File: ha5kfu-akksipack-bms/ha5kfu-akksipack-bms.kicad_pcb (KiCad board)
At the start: 2 copper layers, 47 parts, among them IC2 BQ4050RSMR, J1 PACK, J2 PACK1, J3 PACK2, J4 COM, Q1 AON6512, Q2 AON6512, Q3 2N7002, Q4 AO3400A, Q5 AO3400A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

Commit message: Add initial PCB design
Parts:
- removed 100n1: C, Capacitor_SMD:C_0805_2012Metric_Pad1.18x1.45mm_HandSolder
- removed IC2: BQ4050RSMR, BQ4050:QFN40P400X400X100-33N-D
- added C10: 100n, Capacitor_SMD:C_0603_1608Metric_Pad1.08x0.95mm_HandSolder, B.Cu at (128.3, 124.2)
- added IC1: BQ4050RSMR, Package_DFN_QFN:VQFN-32-1EP_4x4mm_P0.4mm_EP2.8x2.8mm, F.Cu at (123.8, 108.6)
- added R23: 100, Resistor_SMD:R_0603_1608Metric_Pad0.98x0.95mm_HandSolder, B.Cu at (127.5, 126.6)
- C1, C2, C3, C4, C5, C6, C7, C8: footprint Capacitor_SMD:C_0805_2012Metric_Pad1.18x1.45mm_HandSolder -> Capacitor_SMD:C_0603_1608Metric_Pad1.08x0.95mm_HandSolder
- J1: footprint Connector_Wire:SolderWire-0.75sqmm_1x02_P4.8mm_D1.25mm_OD2.3mm -> Connector_AMASS:AMASS_XT30U-F_1x02_P5.0mm_Vertical
- J2, J3: footprint Connector_JST:JST_PH_B3B-PH-K_1x03_P2.00mm_Vertical -> Connector_JST:JST_PH_S3B-PH-K_1x03_P2.00mm_Horizontal
- R1, R22: footprint Resistor_SMD:R_0805_2012Metric_Pad1.20x1.40mm_HandSolder -> Resistor_SMD:R_0603_1608Metric_Pad0.98x0.95mm_HandSolder; moved to B.Cu
- R10, R11, R13, R15, R16, R2, R3, R6, R7: footprint Resistor_SMD:R_0805_2012Metric_Pad1.20x1.40mm_HandSolder -> Resistor_SMD:R_0603_1608Metric_Pad0.98x0.95mm_HandSolder
- R12, R14, R17, R4, R5, R8, R9: footprint Resistor_SMD:R_1206_3216Metric -> Resistor_SMD:R_0603_1608Metric_Pad0.98x0.95mm_HandSolder
- R18: value 100 -> 10k; footprint Resistor_SMD:R_0805_2012Metric_Pad1.20x1.40mm_HandSolder -> Resistor_SMD:R_0603_1608Metric_Pad0.98x0.95mm_HandSolder
- R19: value 33 -> 100; footprint Resistor_SMD:R_1206_3216Metric -> Resistor_SMD:R_0603_1608Metric_Pad0.98x0.95mm_HandSolder
- R20: value 0.001 -> 33; footprint Resistor_SMD:R_1206_3216Metric -> Resistor_SMD:R_0603_1608Metric_Pad0.98x0.95mm_HandSolder
- R21: value 100 -> 0.001; footprint Resistor_SMD:R_0805_2012Metric_Pad1.20x1.40mm_HandSolder -> Resistor_SMD:R_1206_3216Metric_Pad1.30x1.75mm_HandSolder; moved to B.Cu
- moved R3 85.4 mm to (120.7, 116.7)
- moved Q3 79.8 mm to (123.5, 116.7), turned to 0 degrees
- moved R7 72.6 mm to (121.6, 114.1), turned to 180 degrees
- moved R11 72.4 mm to (126.5, 117.0), turned to 90 degrees
- moved R10 71.8 mm to (128.9, 116.1), turned to 180 degrees
- moved R2 69.5 mm to (128.8, 121.5)
- moved Q2 67.8 mm to (133.2, 121.3), turned to 0 degrees
- moved R16 66.5 mm to (120.4, 106.7), turned to 90 degrees
- moved R6 61.4 mm to (128.3, 114.6), turned to 180 degrees
- moved C2 61.4 mm to (135.0, 117.6)
- moved C1 61.1 mm to (139.2, 117.6)
- moved C9 57.8 mm to (127.4, 111.9), turned to -90 degrees
- moved J2 55.9 mm to (139.8, 126.1), turned to 0 degrees
- moved D1 55.5 mm to (132.8, 115.1), turned to 0 degrees
- moved Q1 54.1 mm to (141.1, 121.3), turned to 180 degrees
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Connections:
- J2 pad 1: Net-(D1-A) -> Net-(J2-Pin_1)
- J2 pad 3: Net-(J2-Pin_3) -> Net-(D1-A)
- J3 pad 1: Net-(J2-Pin_3) -> GND
- J3 pad 3: GND -> Net-(J2-Pin_1)
- Q5 pad 2: Net-(J2-Pin_3) -> Net-(J2-Pin_1)
- R12 pad 1: Net-(J2-Pin_3) -> Net-(J2-Pin_1)
- R14 pad 1: Net-(J2-Pin_3) -> Net-(J2-Pin_1)
- R18 pad 1: Net-(IC2-~{PRES}/~{SHDN}) -> GND
- R19 pad 1: Net-(Q7-S) -> Net-(IC1-~{PRES}/~{SHDN})
- R19 pad 2: GND -> /~{SHDN}
- R20 pad 1: GND -> Net-(Q7-S)
- R20 pad 2: /PACK- -> GND
- R21 pad 1: Net-(IC2-SRP) -> GND
- R21 pad 2: GND -> /PACK-
- R22 pad 2: /PACK- -> GND
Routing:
- net Net-(D1-A): track 0.00 -> 35.6 mm, vias 0 -> 2
- net Net-(J2-Pin_1): track 0.00 -> 25.3 mm, vias 0 -> 1
- net Net-(IC1-VC3): track 0.00 -> 23.4 mm, vias 0 -> 2
- net Net-(IC1-SRP): track 0.00 -> 22.7 mm, vias 0 -> 1
- net /PACK+: track 0.00 -> 22.4 mm
- net Net-(Q1-G): track 0.00 -> 21.1 mm, vias 0 -> 2
- net Net-(IC1-VC4): track 0.00 -> 21.1 mm, vias 0 -> 2
- net Net-(IC1-SRN): track 0.00 -> 21.0 mm, vias 0 -> 1
- net GND: track 0.00 -> 19.9 mm, vias 0 -> 7
- net /PACK-: track 0.00 -> 19.4 mm
- net Net-(Q1-D): track 0.00 -> 19.4 mm, vias 0 -> 2
- net Net-(IC1-VC2): track 0.00 -> 19.3 mm, vias 0 -> 2
- net Net-(J2-Pin_2): track 0.00 -> 19.3 mm, vias 0 -> 1
- net Net-(J3-Pin_2): track 0.00 -> 19.1 mm, vias 0 -> 1
- net Net-(IC1-VC1): track 0.00 -> 17.8 mm
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- added copper zone on F.Cu, net /PACK+
- added copper zone on B.Cu, net GND
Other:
- board outline added: 26.6 x 40.7 mm

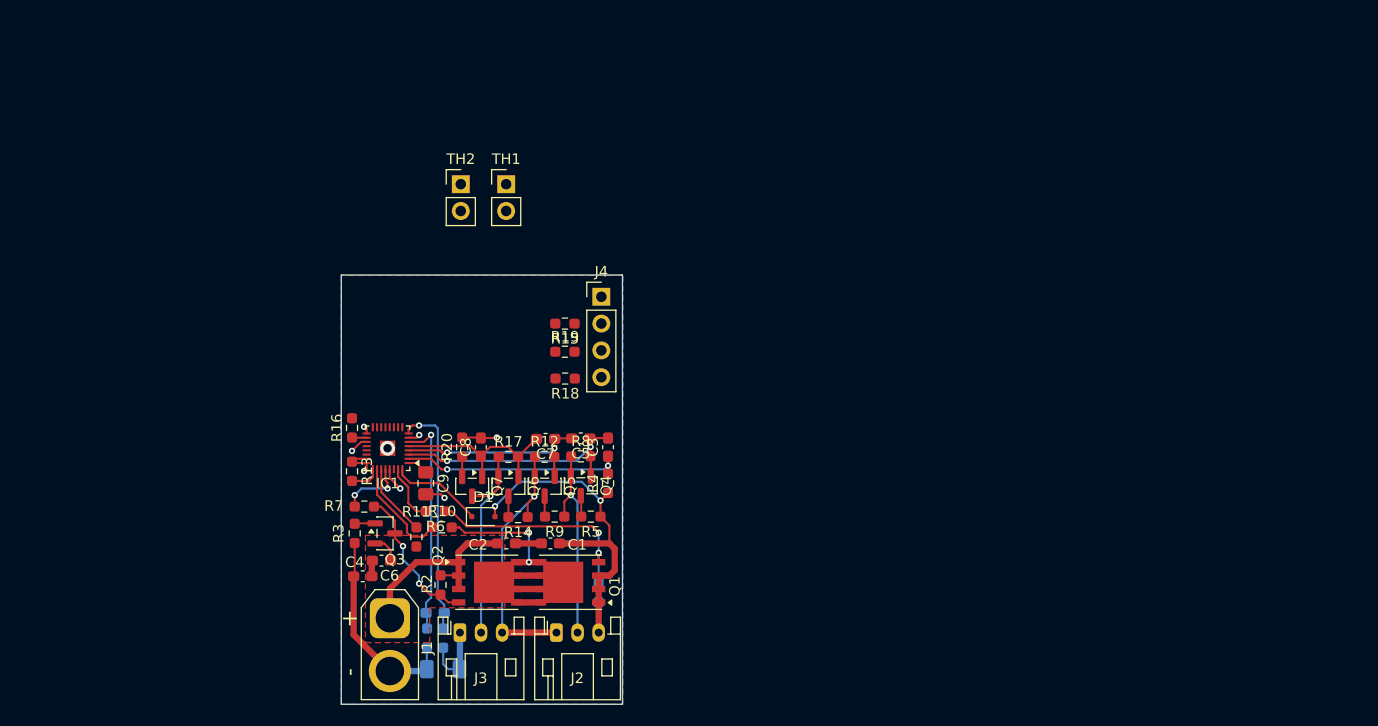
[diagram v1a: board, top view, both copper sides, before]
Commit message: Add LEDs, modify PCB
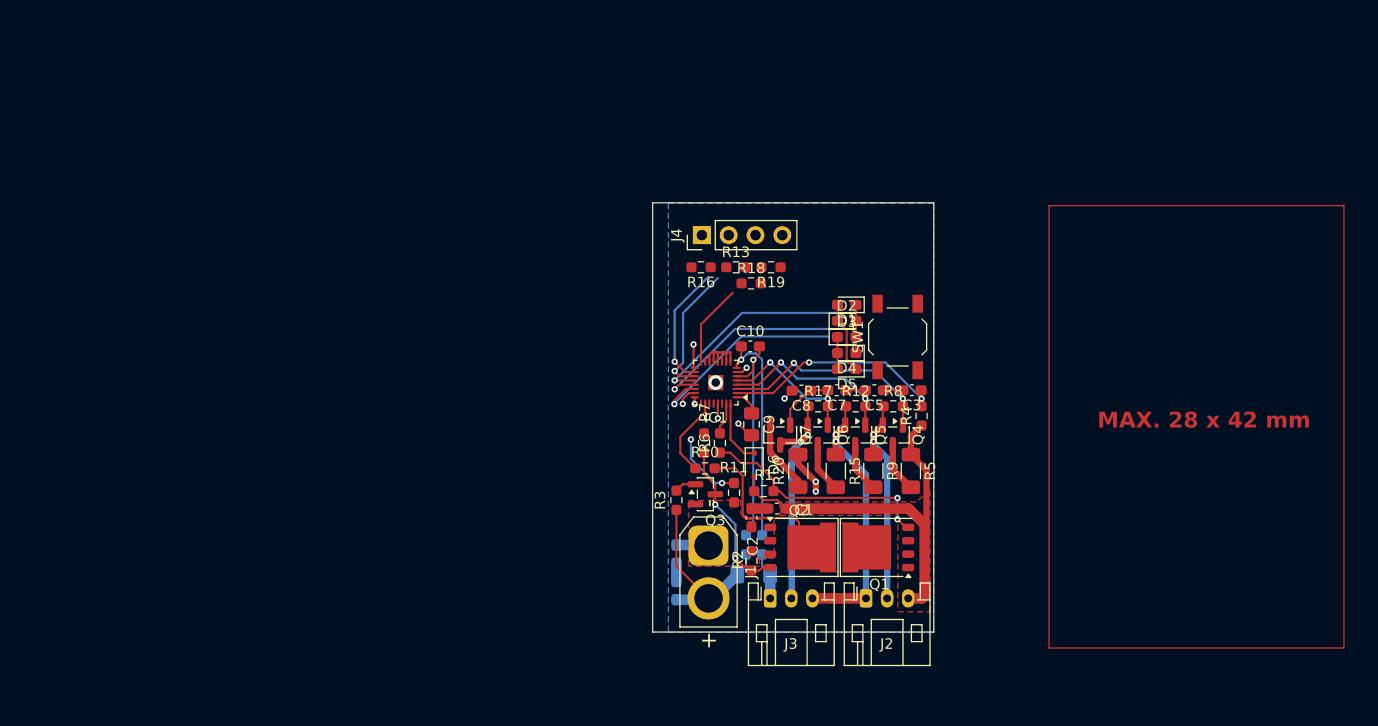
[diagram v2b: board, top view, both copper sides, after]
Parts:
- removed R14: 33, Resistor_SMD:R_0603_1608Metric_Pad0.98x0.95mm_HandSolder
- removed TH1, TH2: 10k -- 3450K, Connector_PinHeader_2.54mm:PinHeader_1x02_P2.54mm_Vertical
- added D2: LED2, LED_SMD:LED_0603_1608Metric_Pad1.05x0.95mm_HandSolder, F.Cu at (167.3, 96.5)
- added D3: LED3, LED_SMD:LED_0603_1608Metric_Pad1.05x0.95mm_HandSolder, F.Cu at (167.3, 98.0)
- added D4: LED4, LED_SMD:LED_0603_1608Metric_Pad1.05x0.95mm_HandSolder, F.Cu at (167.3, 99.6)
- added D5: LED5, LED_SMD:LED_0603_1608Metric_Pad1.05x0.95mm_HandSolder, F.Cu at (167.3, 101.1)
- added D6: BAT54, Diode_SMD:D_SOD-323F, F.Cu at (158.5, 110.2)
- added SW1: DISP, Button_Switch_SMD:SW_SPST_TL3342, F.Cu at (172.1, 98.0)
- C10, R1: moved to F.Cu
- C4, C6: moved to B.Cu
- D1: value BAT54 -> LED1; footprint Diode_SMD:D_SOD-323F -> LED_SMD:LED_0603_1608Metric_Pad1.05x0.95mm_HandSolder
- Q1, Q2: footprint Package_SO:PowerPAK_SO-8_Single -> Package_DFN_QFN:PQFN-8-EP_6x5mm_P1.27mm_Generic
- R11: value 10k -> 10k precision
- R13: value 0 -> 100
- R15: value 100 -> 33; footprint Resistor_SMD:R_0603_1608Metric_Pad0.98x0.95mm_HandSolder -> Resistor_SMD:R_1206_3216Metric_Pad1.30x1.75mm_HandSolder
- R18: value 10k -> 100
- R19: value 100 -> 10k
- R20, R5, R9: footprint Resistor_SMD:R_0603_1608Metric_Pad0.98x0.95mm_HandSolder -> Resistor_SMD:R_1206_3216Metric_Pad1.30x1.75mm_HandSolder
- moved R13 41.2 mm to (156.8, 91.4), turned to 0 degrees
- moved D1 39.8 mm to (167.3, 95.0), turned to 180 degrees
- moved C10 39.1 mm to (158.1, 98.9), turned to 0 degrees
- moved R16 36.4 mm to (153.5, 91.4), turned to 180 degrees
- moved R7 32.7 mm to (153.8, 108.1), turned to 90 degrees
- moved R20 31.9 mm to (162.7, 110.7)
- moved IC1 31.7 mm to (154.9, 102.4)
- moved R23 31.5 mm to (157.7, 117.7)
- moved R22 31.5 mm to (159.3, 117.7)
- moved C9 31.4 mm to (158.2, 106.3)
- moved J1 31.0 mm to (154.2, 117.8)
- moved C8 30.8 mm to (163.0, 103.1), turned to 180 degrees
- moved R21 30.8 mm to (158.5, 120.5)
- moved R3 30.6 mm to (151.1, 113.5)
- moved R5 30.6 mm to (173.3, 110.7), turned to -90 degrees
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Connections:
- net /~{SHDN} renamed /~{PRES}
- C1 pad 1: Net-(D1-A) -> Net-(D6-A)
- IC1 pad 10: Net-(IC1-TS1) -> GND
- IC1 pad 11: Net-(IC1-TS2) -> GND
- IC1 pad 17: GND -> Net-(IC1-~{DISP})
- IC1 pad 20: unconnected-(IC1-LEDCNTLA-Pad20) -> Net-(D1-A)
- IC1 pad 21: unconnected-(IC1-LEDCNTLB-Pad21) -> Net-(D1-K)
- IC1 pad 22: unconnected-(IC1-LEDCNTLC-Pad22) -> Net-(D3-K)
- IC1 pad 25: Net-(IC1-FUSE) -> unconnected-(IC1-FUSE-Pad25)
- IC1 pad 32: Net-(D1-K) -> Net-(D6-K)
- J2 pad 3: Net-(D1-A) -> Net-(D6-A)
- Q1 pad 1: Net-(D1-A) -> Net-(D6-A)
- Q1 pad 2: Net-(D1-A) -> Net-(D6-A)
- Q1 pad 3: Net-(D1-A) -> Net-(D6-A)
- R1 pad 1: Net-(D1-A) -> Net-(D6-A)
- R13 pad 1: GND -> /SMB_SCL
- R13 pad 2: Net-(IC1-FUSE) -> Net-(IC1-SMBC)
- R15 pad 1: /SMB_SCL -> Net-(J2-Pin_1)
- R15 pad 2: Net-(IC1-SMBC) -> Net-(Q6-D)
- R18 pad 1: GND -> Net-(IC1-~{PRES}/~{SHDN})
- R19 pad 1: Net-(IC1-~{PRES}/~{SHDN}) -> GND
- R4 pad 1: Net-(D1-A) -> Net-(D6-A)
- R5 pad 1: Net-(D1-A) -> Net-(D6-A)
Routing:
- net Net-(D6-A): track 0.00 -> 37.7 mm
- net Net-(D3-K): track 0.00 -> 23.1 mm, vias 0 -> 1
- net /PACK+: track 22.4 -> 3.07 mm
- net Net-(D1-K): track 8.81 -> 26.2 mm, vias 0 -> 1
- net Net-(IC1-SMBC): track 1.73 -> 12.6 mm
- net Net-(IC1-SMBD): track 1.39 -> 11.7 mm, vias 0 -> 1
- net Net-(D1-A): track 35.6 -> 26.7 mm, vias 2 -> 1
- net Net-(IC1-~{PRES}/~{SHDN}): track 0.00 -> 7.77 mm
- net Net-(IC1-DSG): track 6.37 -> 0.00 mm, vias 2 -> 0
- net Net-(D6-K): track 0.00 -> 6.19 mm
- net Net-(Q7-S): track 1.86 -> 7.00 mm
- net Net-(Q1-D): track 19.4 -> 14.6 mm, vias 2 -> 0
- net GND: track 19.9 -> 23.6 mm, vias 7 -> 9
- net Net-(IC1-FUSE): track 2.86 -> 0.00 mm
- net Net-(J3-Pin_2): track 19.1 -> 21.9 mm, vias 1 -> 2
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- added copper zone on F.Cu, net Net-(D6-A)
- added copper zone on F.Cu, net Net-(Q1-D)
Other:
- board text added: "MAX. 28 x 42 mm"

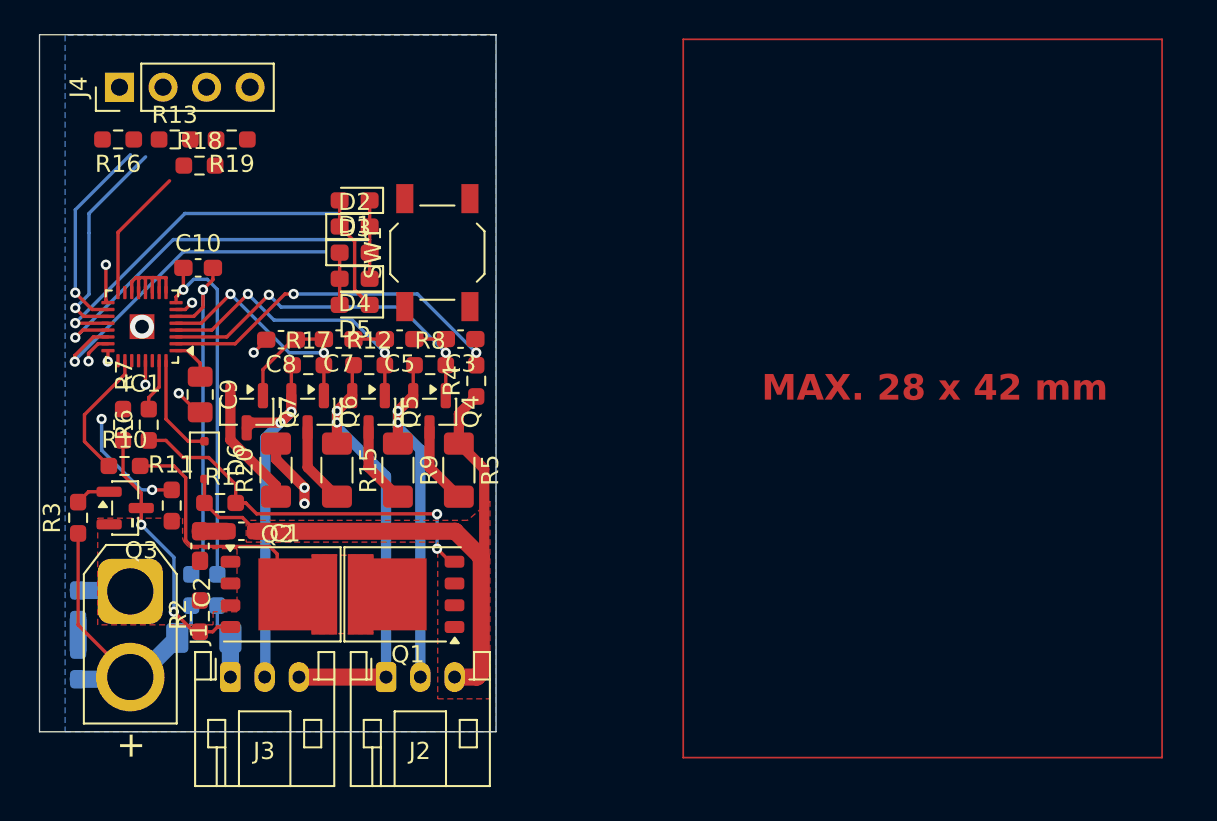
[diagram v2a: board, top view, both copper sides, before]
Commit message: Complete PCB, add comments (as documentation) to schematic
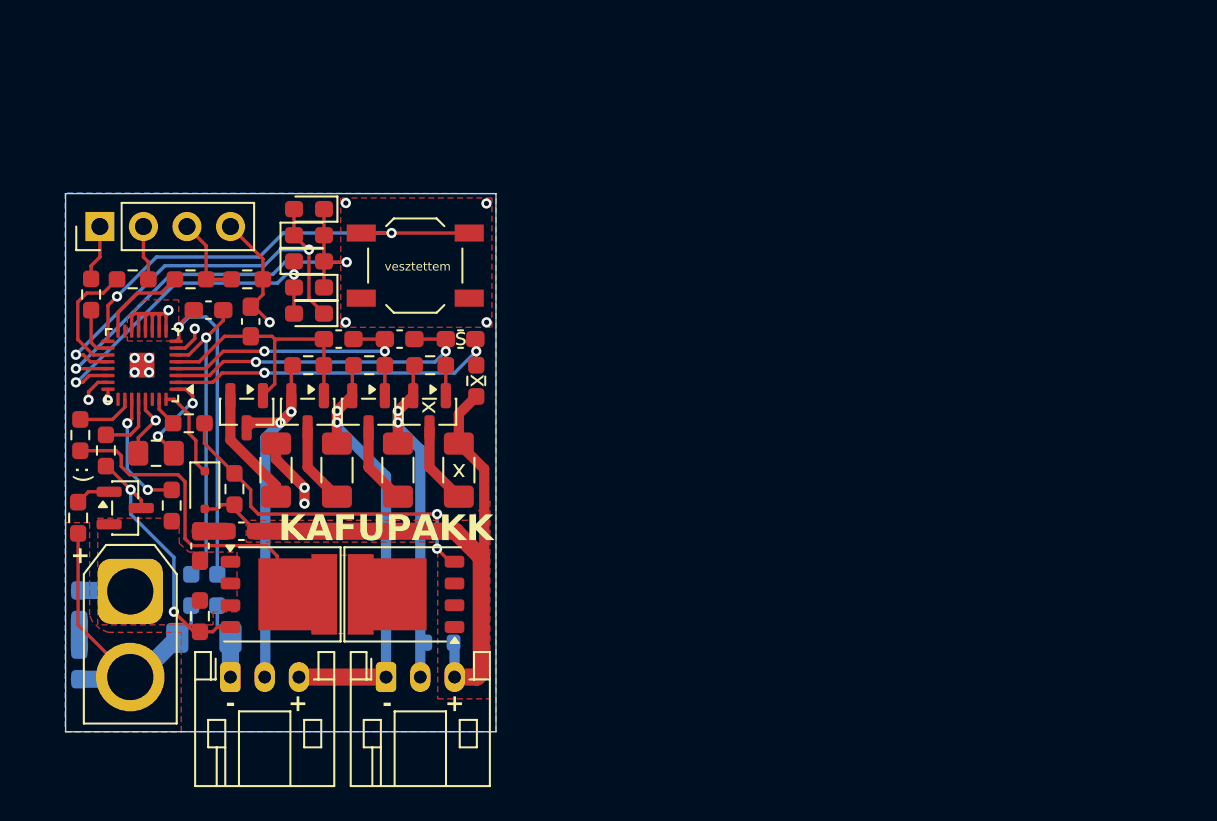
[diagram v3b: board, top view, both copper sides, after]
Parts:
- added BT1: LiFePO4, Resistor_SMD:R_0603_1608Metric, B.Cu at (172.2, 120.8)
- moved R16 9.18 mm to (151.9, 100.5), turned to 90 degrees
- moved R13 8.52 mm to (154.3, 99.6), turned to 180 degrees
- moved R19 8.21 mm to (161.0, 99.6)
- moved J4 8.21 mm to (152.4, 96.5)
- moved R18 6.66 mm to (157.7, 99.6)
- moved C9 4.29 mm to (155.7, 109.8), turned to 180 degrees
- moved R10 3.15 mm to (151.3, 108.7), turned to 90 degrees
- moved D1 2.71 mm to (164.6, 95.5)
- moved D2 2.71 mm to (164.6, 97.0)
- moved D3 2.71 mm to (164.6, 98.6)
- moved D4 2.71 mm to (164.6, 100.1)
- moved D5 2.71 mm to (164.6, 101.6)
- moved C10 2.54 mm to (158.7, 101.4)
- moved R6 2.34 mm to (157.6, 108.0), turned to 180 degrees
- moved IC1 2.25 mm to (154.9, 104.6)
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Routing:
- net Net-(IC1-~{DISP}): track 2.26 -> 26.7 mm, vias 1 -> 2
- net GND: track 23.6 -> 33.2 mm, vias 9 -> 16
- net Net-(IC1-SMBD): track 11.7 -> 3.00 mm, vias 1 -> 0
- net Net-(IC1-SMBC): track 12.6 -> 7.16 mm, vias 1 -> 0
- net /~{PRES}: track 0.00 -> 5.03 mm
- net Net-(IC1-VCC): track 7.71 -> 3.36 mm
- net Net-(Q1-D): track 14.6 -> 18.6 mm
- net Net-(IC1-DSG): track 0.00 -> 3.80 mm
- net Net-(IC1-VC1): track 19.9 -> 16.2 mm, vias 2 -> 0
- net Net-(IC1-PBI): track 2.49 -> 5.91 mm, vias 0 -> 2
- net /SMB_SDA: track 0.00 -> 3.27 mm
- net /SMB_SCL: track 0.00 -> 3.20 mm
- net Net-(IC1-SRN): track 21.2 -> 18.4 mm
- net Net-(D3-K): track 23.1 -> 20.4 mm, vias 1 -> 2
- net Net-(IC1-~{PRES}/~{SHDN}): track 7.77 -> 5.20 mm
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- added copper zone on F.Cu, net /PACK-
- added copper zone on F.Cu, net GND
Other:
- board size 26.6 x 40.7 mm -> 25.1 x 31.4 mm
- board text added: "+"
- board text added: "-"
- board text added: "....."
- board text added: ":)"
- board text added: "GND"
- board text added: "In a 3-series configuration: - DNP components marked with X - short components marked with S"
- board text added: "KAFUPAKK"
- board text added: "P+"
- board text added: "P-"
- board text added: "PCB DE HA3PB 2026"
- board text added: "SMBC"
- board text added: "SMBD"
- board text added: "s"
- board text added: "vesztettem"
- board text added: "x"
- board text added: "~{PRES}"
- board text removed: "MAX. 28 x 42 mm"
